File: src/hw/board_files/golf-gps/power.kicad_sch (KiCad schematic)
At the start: 31 parts, among them P1 USB_C_Plug_USB2.0, SW1 SW_SPDT, U1 FT234XD-R, U2 MCP73831-2-OT, U3 TPS63031DSKR

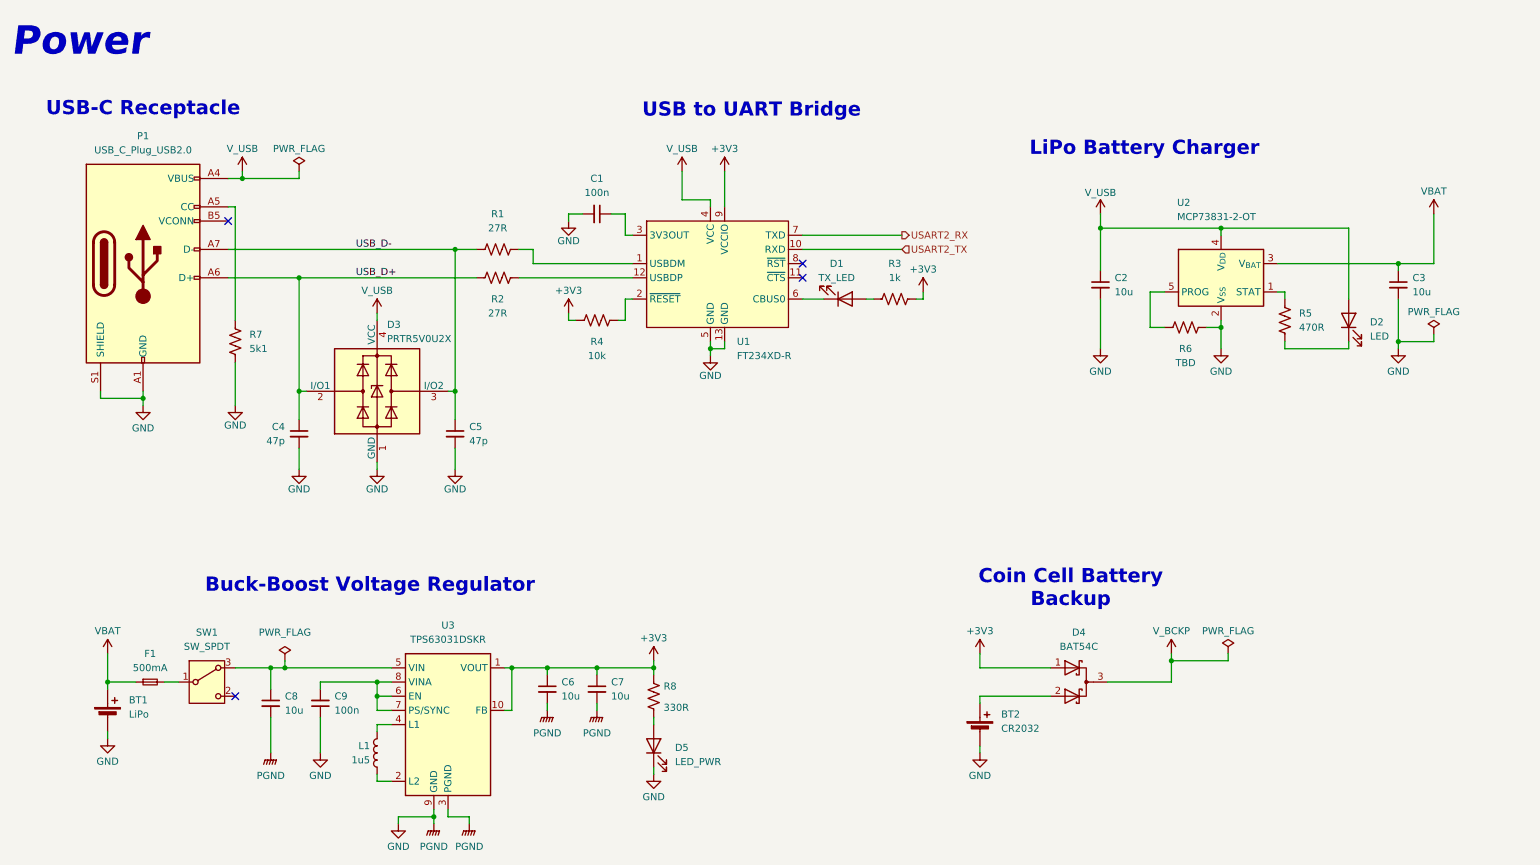
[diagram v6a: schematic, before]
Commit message: Removed USB to UART bridge, added VDDA decoupling, adjusted MCU pinout and updated spreadsheet
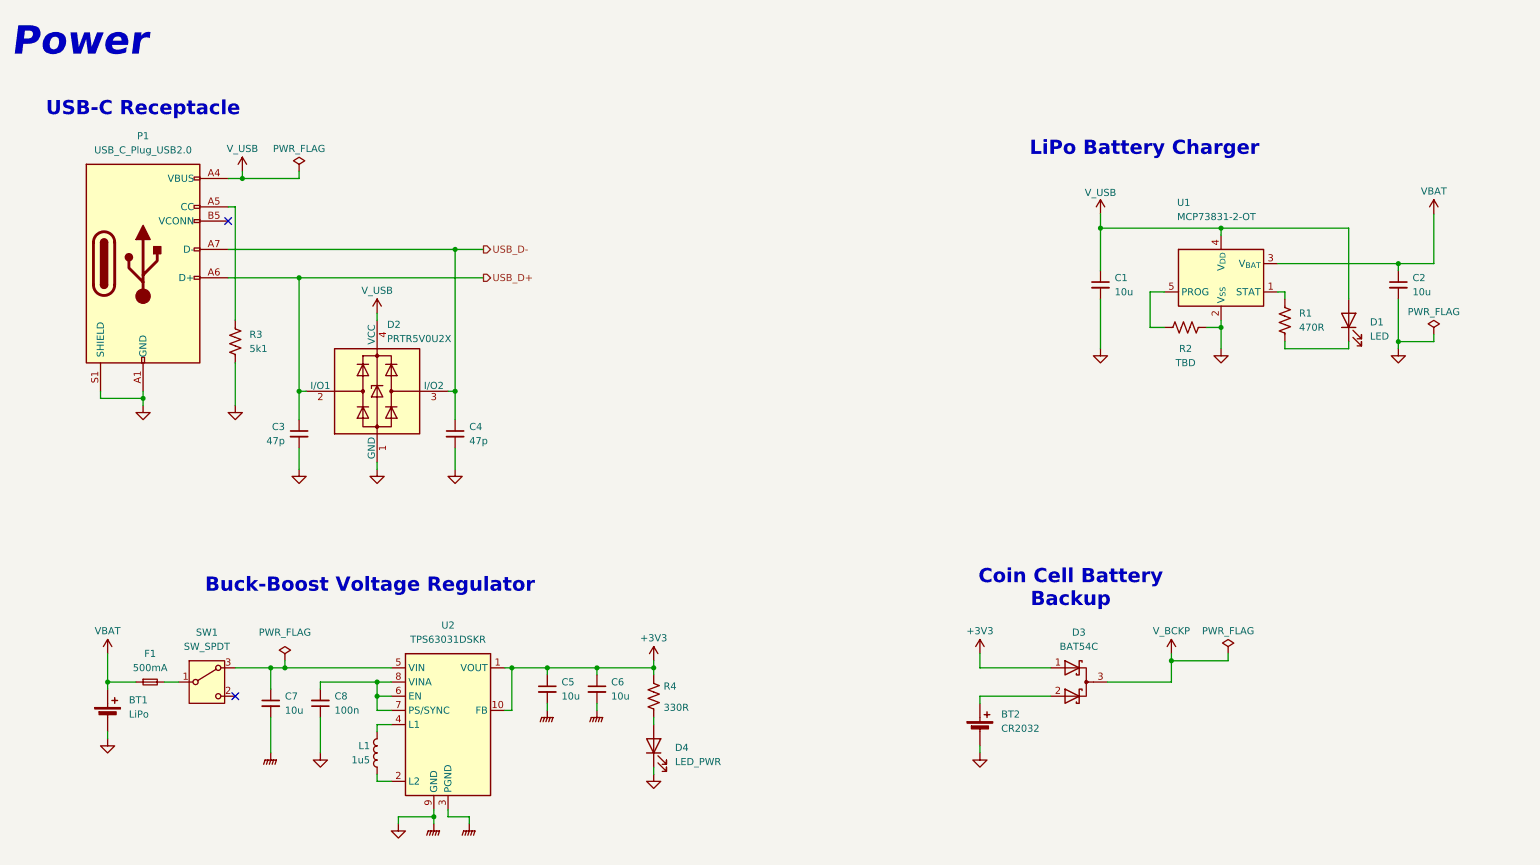
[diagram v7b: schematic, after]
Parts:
- removed C1: 100n, Capacitor_SMD:C_0603_1608Metric, symbol Device:C_Small
- removed D1: TX_LED, LED_SMD:LED_0603_1608Metric, symbol Device:LED
- removed R1, R2: 27R, Resistor_SMD:R_0603_1608Metric, symbol Device:R_US
- removed R3: 1k, Resistor_SMD:R_0603_1608Metric, symbol Device:R_US
- removed R4: 10k, Resistor_SMD:R_0603_1608Metric, symbol Device:R_US
- removed U1: FT234XD-R, Package_DFN_QFN:DFN-12-1EP_3x3mm_P0.45mm_EP1.65x2.38mm, symbol smart_clock:FT234XD-R
- BT2: footprint Battery:BatteryHolder_Keystone_3034_1x20mm -> Battery:BatteryHolder_Keystone_3002_1x2032
- renumbered C2 to C1, C3 to C2, C4 to C3, C5 to C4, C6 to C5, C7 to C6, C8 to C7, C9 to C8, D2 to D1, D3 to D2, D4 to D3, D5 to D4, R5 to R1, R6 to R2, R7 to R3, R8 to R4, U2 to U1, U3 to U2
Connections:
- no-connect marks 4 -> 2
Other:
- note removed: "USB to UART Bridge"

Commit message: Updated pinout and spreadsheet, PCB changes
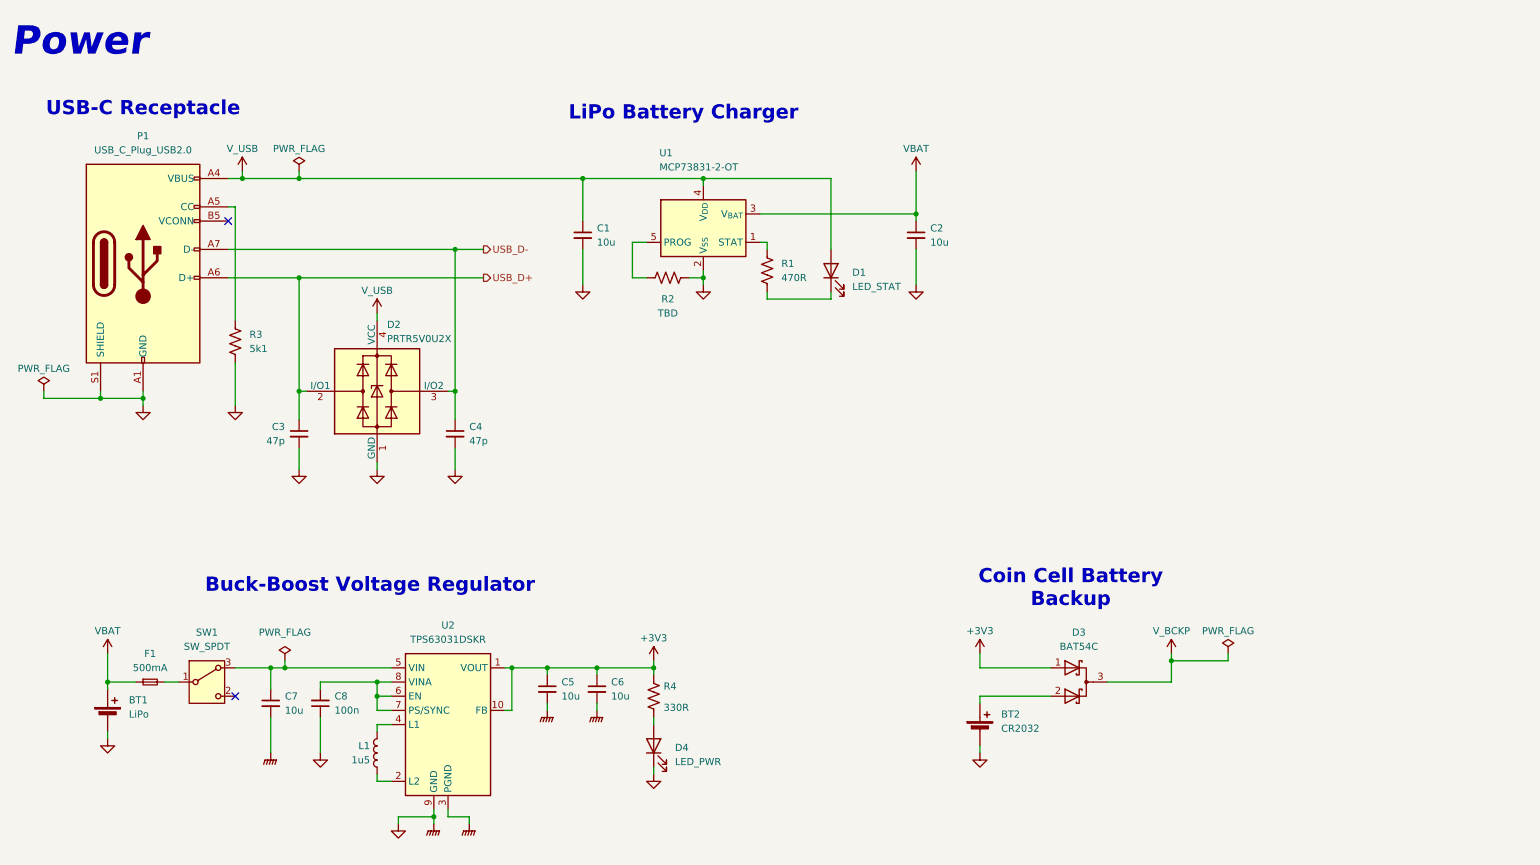
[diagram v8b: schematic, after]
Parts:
- D1: value LED -> LED_STAT
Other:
- moved on the sheet: C1, C2, D1, R1, R2, U1
